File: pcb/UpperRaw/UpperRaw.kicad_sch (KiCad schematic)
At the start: 17 parts, among them J1 Conn_01x04, SW100 SW_DPDT_x2, SW101 SW_DPDT_x2, SW102 SW_SPDT, SW103 SW_SPDT

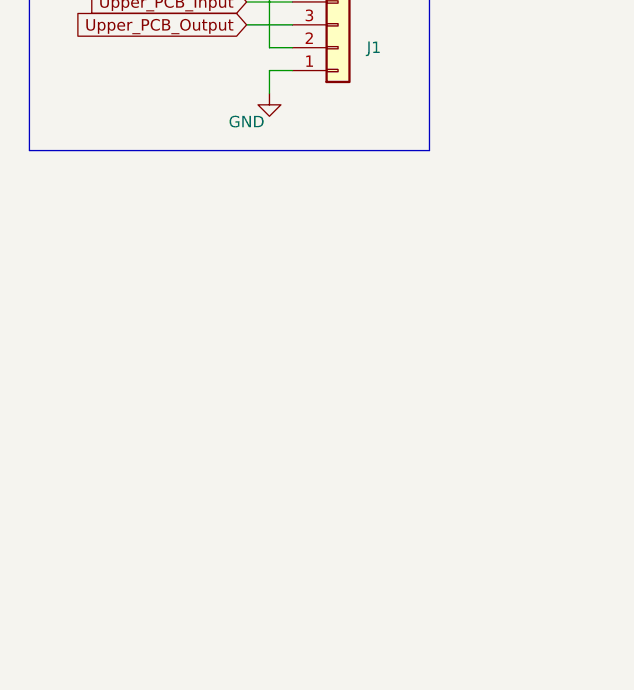
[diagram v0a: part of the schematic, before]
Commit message: [UpperRaw] Add symbols from 404 PCB
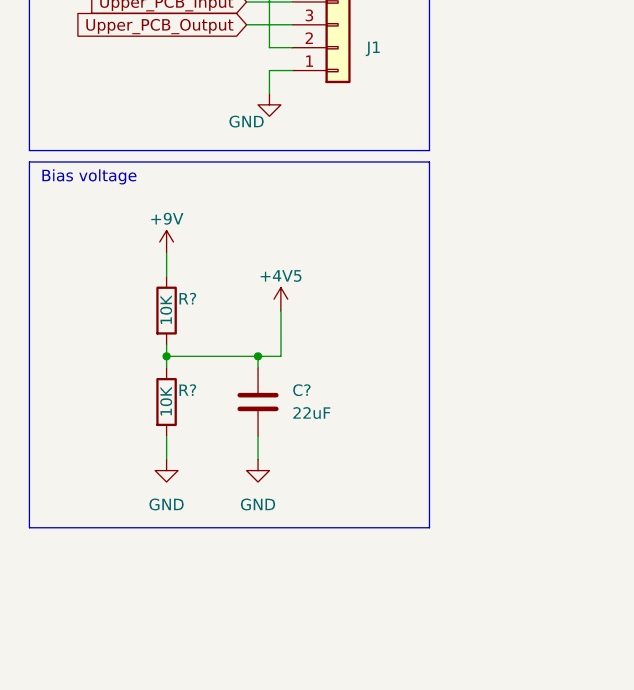
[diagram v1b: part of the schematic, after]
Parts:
- added C?: 22uF, Capacitor_SMD:C_1206_3216Metric, symbol Device:C
- added R? (x2): 10K, Resistor_SMD:R_0603_1608Metric, symbol Device:R
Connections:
- net +9V: now also R?.1
- net GND: now also C?.2, R?.2
- new net +4V5: C?.1, R?.1, R?.2
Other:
- note added: "Bias voltage"
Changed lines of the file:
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@@
     (company "Binary-6")
   )
+  (junction (at 29.21 63.5) (diameter 0) (color 0 0 0 0)
+  )
+  (junction (at 39.37 63.5) (diameter 0) (color 0 0 0 0)
+  )
   (polyline (pts (xy 58.42 40.64) (xy 58.42 13.97))
     (stroke (width 0) (type default) (color 0 0 0 0))
@@
     (stroke (width 0) (type default) (color 0 0 0 0))
   )
+  (wire (pts (xy 29.21 63.5) (xy 39.37 63.5))
+    (stroke (width 0) (type default) (color 0 0 0 0))
+  )
+  (polyline (pts (xy 13.97 82.55) (xy 58.42 82.55))
+    (stroke (width 0) (type default) (color 0 0 0 0))
+  )
   (wire (pts (xy 40.64 21.59) (xy 40.64 29.21))
     (stroke (width 0) (type default) (color 0 0 0 0))
   )
+  (wire (pts (xy 41.91 63.5) (xy 39.37 63.5))
+    (stroke (width 0) (type default) (color 0 0 0 0))
+  )
+  (wire (pts (xy 29.21 62.23) (xy 29.21 63.5))
+    (stroke (width 0) (type default) (color 0 0 0 0))
+  )
+  (wire (pts (xy 29.21 72.39) (xy 29.21 74.93))
+    (stroke (width 0) (type default) (color 0 0 0 0))
+  )
   (polyline (pts (xy 13.97 40.64) (xy 58.42 40.64))
     (stroke (width 0) (type default) (color 0 0 0 0))
   )
+  (polyline (pts (xy 13.97 41.91) (xy 13.97 82.55))
+    (stroke (width 0) (type default) (color 0 0 0 0))
+  )
   (polyline (pts (xy 58.42 13.97) (xy 13.97 13.97))
     (stroke (width 0) (type default) (color 0 0 0 0))
   )
+  (wire (pts (xy 29.21 63.5) (xy 29.21 64.77))
+    (stroke (width 0) (type default) (color 0 0 0 0))
+  )
+  (wire (pts (xy 29.21 52.07) (xy 29.21 54.61))
+    (stroke (width 0) (type default) (color 0 0 0 0))
+  )
   (polyline (pts (xy 12.7 149.86) (xy 12.7 196.85))
     (stroke (width 0) (type default) (color 0 0 0 0))
@@
     (stroke (width 0) (type default) (color 0 0 0 0))
   )
+  (wire (pts (xy 39.37 72.39) (xy 39.37 74.93))
+    (stroke (width 0) (type default) (color 0 0 0 0))
+  )
   (wire (pts (xy 40.64 31.75) (xy 40.64 34.29))
     (stroke (width 0) (type default) (color 0 0 0 0))
@@
     (stroke (width 0) (type default) (color 0 0 0 0))
   )
+  (polyline (pts (xy 58.42 41.91) (xy 58.42 82.55))
+    (stroke (width 0) (type default) (color 0 0 0 0))
+  )
+  (wire (pts (xy 41.91 58.42) (xy 41.91 63.5))
+    (stroke (width 0) (type default) (color 0 0 0 0))
+  )
   (wire (pts (xy 38.1 24.13) (xy 43.18 24.13))
     (stroke (width 0) (type default) (color 0 0 0 0))
   )
+  (wire (pts (xy 39.37 63.5) (xy 39.37 64.77))
+    (stroke (width 0) (type default) (color 0 0 0 0))
+  )
   (polyline (pts (xy 12.7 149.86) (xy 134.62 149.86))
     (stroke (width 0) (type default) (color 0 0 0 0))
   )
+  (polyline (pts (xy 58.42 41.91) (xy 13.97 41.91))
+    (stroke (width 0) (type default) (color 0 0 0 0))
+  )
   (polyline (pts (xy 134.62 149.86) (xy 134.62 196.85))
     (stroke (width 0) (type default) (color 0 0 0 0))
@@
   (polyline (pts (xy 13.97 13.97) (xy 13.97 40.64))
     (stroke (width 0) (type default) (color 0 0 0 0))
+  )
+  (text "Bias voltage" (at 15.24 44.45 0)
+    (effects (font (size 1.27 1.27)) (justify left bottom))
   )
   (text "Lower to Upper PCB connector" (at 14.605 16.51 0)
@@
     (pin "1")
   )
+  (symbol (lib_id "power:GND") (at 39.37 74.93 0) (unit 1)
+    (in_bom yes) (on_board yes)
+    (property "Reference" "#PWR?" (id 0) (at 39.37 81.28 0)
+      (effects (font (size 1.27 1.27)) hide)
+    )
+    (property "Value" "GND" (id 1) (at 39.37 80.01 0))
+    (property "Footprint" "" (id 2) (at 39.37 74.93 0)
+      (effects (font (size 1.27 1.27)) hide)
+    )
+    (property "Datasheet" "" (id 3) (at 39.37 74.93 0)
+      (effects (font (size 1.27 1.27)) hide)
+    )
+    (pin "1")
+  )
   (symbol (lib_id "Switch:SW_SPDT") (at 120.65 161.29 0) (unit 1)
     (in_bom yes) (on_board yes) (fields_autoplaced)
@@
     (pin "2")
   )
+  (symbol (lib_id "power:+9V") (at 29.21 52.07 0) (unit 1)
+    (in_bom yes) (on_board yes)
+    (property "Reference" "#PWR?" (id 0) (at 29.21 55.88 0)
+      (effects (font (size 1.27 1.27)) hide)
+    )
+    (property "Value" "+9V" (id 1) (at 29.21 48.26 0))
+    (property "Footprint" "" (id 2) (at 29.21 52.07 0)
+      (effects (font (size 1.27 1.27)) hide)
+    )
+    (property "Datasheet" "" (id 3) (at 29.21 52.07 0)
+      (effects (font (size 1.27 1.27)) hide)
+    )
+    (pin "1")
+  )
   (symbol (lib_id "Switch:SW_DPDT_x2") (at 87.63 173.99 0) (unit 2)
     (in_bom yes) (on_board yes) (fields_autoplaced)
@@
     (pin "1")
   )
+  (symbol (lib_id "Device:R") (at 29.21 58.42 0) (unit 1)
+    (in_bom yes) (on_board yes)
+    (property "Reference" "R?" (id 0) (at 30.48 57.15 0)
+      (effects (font (size 1.27 1.27)) (justify left))
+    )
+    (property "Value" "10K" (id 1) (at 29.21 58.42 90))
+    (property "Footprint" "Resistor_SMD:R_0603_1608Metric" (id 2) (at 27.432 58.42 90)
+      (effects (font (size 1.27 1.27)) hide)
+    )
+    (property "Datasheet" "~" (id 3) (at 29.21 58.42 0)
+      (effects (font (size 1.27 1.27)) hide)
+    )
+    (property "LCSC" "C25804" (id 4) (at 29.21 58.42 0)
+      (effects (font (size 1.27 1.27)) hide)
+    )
+    (pin "1")
+    (pin "2")
+  )
   (symbol (lib_id "Device:C") (at 36.83 180.34 0) (mirror y) (unit 1)
     (in_bom yes) (on_board yes) (fields_autoplaced)
@@
     (pin "2")
   )
+  (symbol (lib_id "Device:C") (at 39.37 68.58 0) (unit 1)
+    (in_bom yes) (on_board yes) (fields_autoplaced)
+    (property "Reference" "C?" (id 0) (at 43.18 67.3099 0)
+      (effects (font (size 1.27 1.27)) (justify left))
+    )
+    (property "Value" "22uF" (id 1) (at 43.18 69.8499 0)
+      (effects (font (size 1.27 1.27)) (justify left))
+    )
+    (property "Footprint" "Capacitor_SMD:C_1206_3216Metric" (id 2) (at 40.3352 72.39 0)
+      (effects (font (size 1.27 1.27)) hide)
+    )
+    (property "Datasheet" "~" (id 3) (at 39.37 68.58 0)
+      (effects (font (size 1.27 1.27)) hide)
+    )
+    (property "LCSC" "C12891" (id 4) (at 39.37 68.58 0)
+      (effects (font (size 1.27 1.27)) hide)
+    )
+    (pin "1")
+    (pin "2")
+  )
+  (symbol (lib_id "Device:R") (at 29.21 68.58 0) (unit 1)
+    (in_bom yes) (on_board yes)
+    (property "Reference" "R?" (id 0) (at 30.48 67.31 0)
+      (effects (font (size 1.27 1.27)) (justify left))
+    )
+    (property "Value" "10K" (id 1) (at 29.21 68.58 90))
+    (property "Footprint" "Resistor_SMD:R_0603_1608Metric" (id 2) (at 27.432 68.58 90)
+      (effects (font (size 1.27 1.27)) hide)
+    )
+    (property "Datasheet" "~" (id 3) (at 29.21 68.58 0)
+      (effects (font (size 1.27 1.27)) hide)
+    )
+    (property "LCSC" "C25804" (id 4) (at 29.21 68.58 0)
+      (effects (font (size 1.27 1.27)) hide)
+    )
+    (pin "1")
+    (pin "2")
+  )
   (symbol (lib_id "power:+9V") (at 16.51 162.56 0) (unit 1)
     (in_bom yes) (on_board yes)
@@
     (pin "1")
     (pin "2")
+  )
+  (symbol (lib_id "power:GND") (at 29.21 74.93 0) (unit 1)
+    (in_bom yes) (on_board yes)
+    (property "Reference" "#PWR?" (id 0) (at 29.21 81.28 0)
+      (effects (font (size 1.27 1.27)) hide)
+    )
+    (property "Value" "GND" (id 1) (at 29.21 80.01 0))
+    (property "Footprint" "" (id 2) (at 29.21 74.93 0)
+      (effects (font (size 1.27 1.27)) hide)
+    )
+    (property "Datasheet" "" (id 3) (at 29.21 74.93 0)
+      (effects (font (size 1.27 1.27)) hide)
+    )
+    (pin "1")
+  )
+  (symbol (lib_id "MeineBibli:+4V5") (at 41.91 58.42 0) (unit 1)
+    (in_bom yes) (on_board yes)
+    (property "Reference" "#PWR?" (id 0) (at 41.91 62.23 0)
+      (effects (font (size 1.27 1.27)) hide)
+    )
+    (property "Value" "+4V5" (id 1) (at 41.91 54.61 0))
+    (property "Footprint" "" (id 2) (at 41.91 58.42 0)
+      (effects (font (size 1.27 1.27)) hide)
+    )
+    (property "Datasheet" "" (id 3) (at 41.91 58.42 0)
+      (effects (font (size 1.27 1.27)) hide)
+    )
+    (pin "1")
   )
   (symbol (lib_id "power:GND") (at 16.51 168.91 0) (unit 1)
@@
       (reference "#PWR04") (unit 1) (value "GND") (footprint "")
     )
+    (path "/09433d97-62ec-42de-89f2-7d0b68dc1b9d"
+      (reference "#PWR?") (unit 1) (value "GND") (footprint "")
+    )
+    (path "/296b967f-b7a9-453f-856a-7b874fdca3db"
+      (reference "#PWR?") (unit 1) (value "+9V") (footprint "")
+    )
+    (path "/b9272e8b-2d00-4d6b-ae8c-fd62ef331586"
+      (reference "#PWR?") (unit 1) (value "GND") (footprint "")
+    )
+    (path "/c2d81a3b-9b02-4ddc-9c7b-c0e881678970"
+      (reference "#PWR?") (unit 1) (value "+4V5") (footprint "")
+    )
     (path "/75f89342-e5fb-4ec8-a9a1-4514a000c1c5"
       (reference "C100") (unit 1) (value "100uF") (footprint "Capacitor_THT:CP_Radial_D5.0mm_P2.00mm")
@@
       (reference "C102") (unit 1) (value "220nF") (footprint "Capacitor_SMD:C_0603_1608Metric")
     )
+    (path "/8672a05d-b750-4ddd-a92d-4c58fddcdd4e"
+      (reference "C?") (unit 1) (value "22uF") (footprint "Capacitor_SMD:C_1206_3216Metric")
+    )
     (path "/43624bd7-5b28-4455-bedf-a59e39f0128d"
       (reference "J1") (unit 1) (value "Conn_01x04") (footprint "Connector_JST:JST_XH_B4B-XH-A_1x04_P2.50mm_Vertical")
@@
       (reference "R103") (unit 1) (value "2k2") (footprint "Resistor_SMD:R_0603_1608Metric")
     )
+    (path "/4e944601-14c5-4478-a9d6-8d2ad19dcc43"
+      (reference "R?") (unit 1) (value "10K") (footprint "Resistor_SMD:R_0603_1608Metric")
+    )
+    (path "/8d9ea4cf-1047-42af-bf72-13258f22d6ad"
+      (reference "R?") (unit 1) (value "10K") (footprint "Resistor_SMD:R_0603_1608Metric")
+    )
     (path "/eade452d-0fd2-478e-ba2c-c8c7cc57b518"

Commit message: [All] Add LCSC part number for JST connector
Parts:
- J1: value Conn_01x04 -> (none); footprint Connector_JST:JST_XH_B4B-XH-A_1x04_P2.50mm_Vertical -> (none); LCSC (none) -> C144395; now in the parts list
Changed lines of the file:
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@@
     (pin "2")
     (pin "3")
+    (pin "4")
+    (pin "5")
+    (pin "6")
   )
   (symbol (lib_id "Device:R") (at 50.8 180.34 0) (unit 1)
@@
       (effects (font (size 1.27 1.27)) hide)
     )
+    (pin "1")
+    (pin "2")
+    (pin "3")
     (pin "4")
     (pin "5")
@@
   )
   (symbol (lib_id "Connector_Generic:Conn_01x04") (at 48.26 29.21 0) (mirror x) (unit 1)
-    (in_bom no) (on_board yes)
+    (in_bom yes) (on_board yes)
     (property "Reference" "J1" (id 0) (at 51.435 29.2101 0)
       (effects (font (size 1.27 1.27)) (justify left))
     )
-    (property "Value" "Conn_01x04" (id 1) (at 44.45 21.59 0)
-      (effects (font (size 1.27 1.27)) (justify left))
-    )
-    (property "Footprint" "Connector_JST:JST_XH_B4B-XH-A_1x04_P2.50mm_Vertical" (id 2) (at 48.26 29.21 0)
+    (property "Value" "" (id 1) (at 44.45 21.59 0)
+      (effects (font (size 1.27 1.27)) (justify left))
+    )
+    (property "Footprint" "" (id 2) (at 48.26 29.21 0)
       (effects (font (size 1.27 1.27)) hide)
     )
     (property "Datasheet" "~" (id 3) (at 48.26 29.21 0)
+      (effects (font (size 1.27 1.27)) hide)
+    )
+    (property "LCSC" "C144395" (id 4) (at 48.26 29.21 0)
       (effects (font (size 1.27 1.27)) hide)
     )
@@
       (effects (font (size 1.27 1.27)) hide)
     )
+    (pin "1")
+    (pin "2")
+    (pin "3")
     (pin "4")
     (pin "5")
@@
     (pin "2")
     (pin "3")
+    (pin "4")
+    (pin "5")
+    (pin "6")
   )
   (symbol (lib_id "power:+9V") (at 40.64 21.59 0) (unit 1)

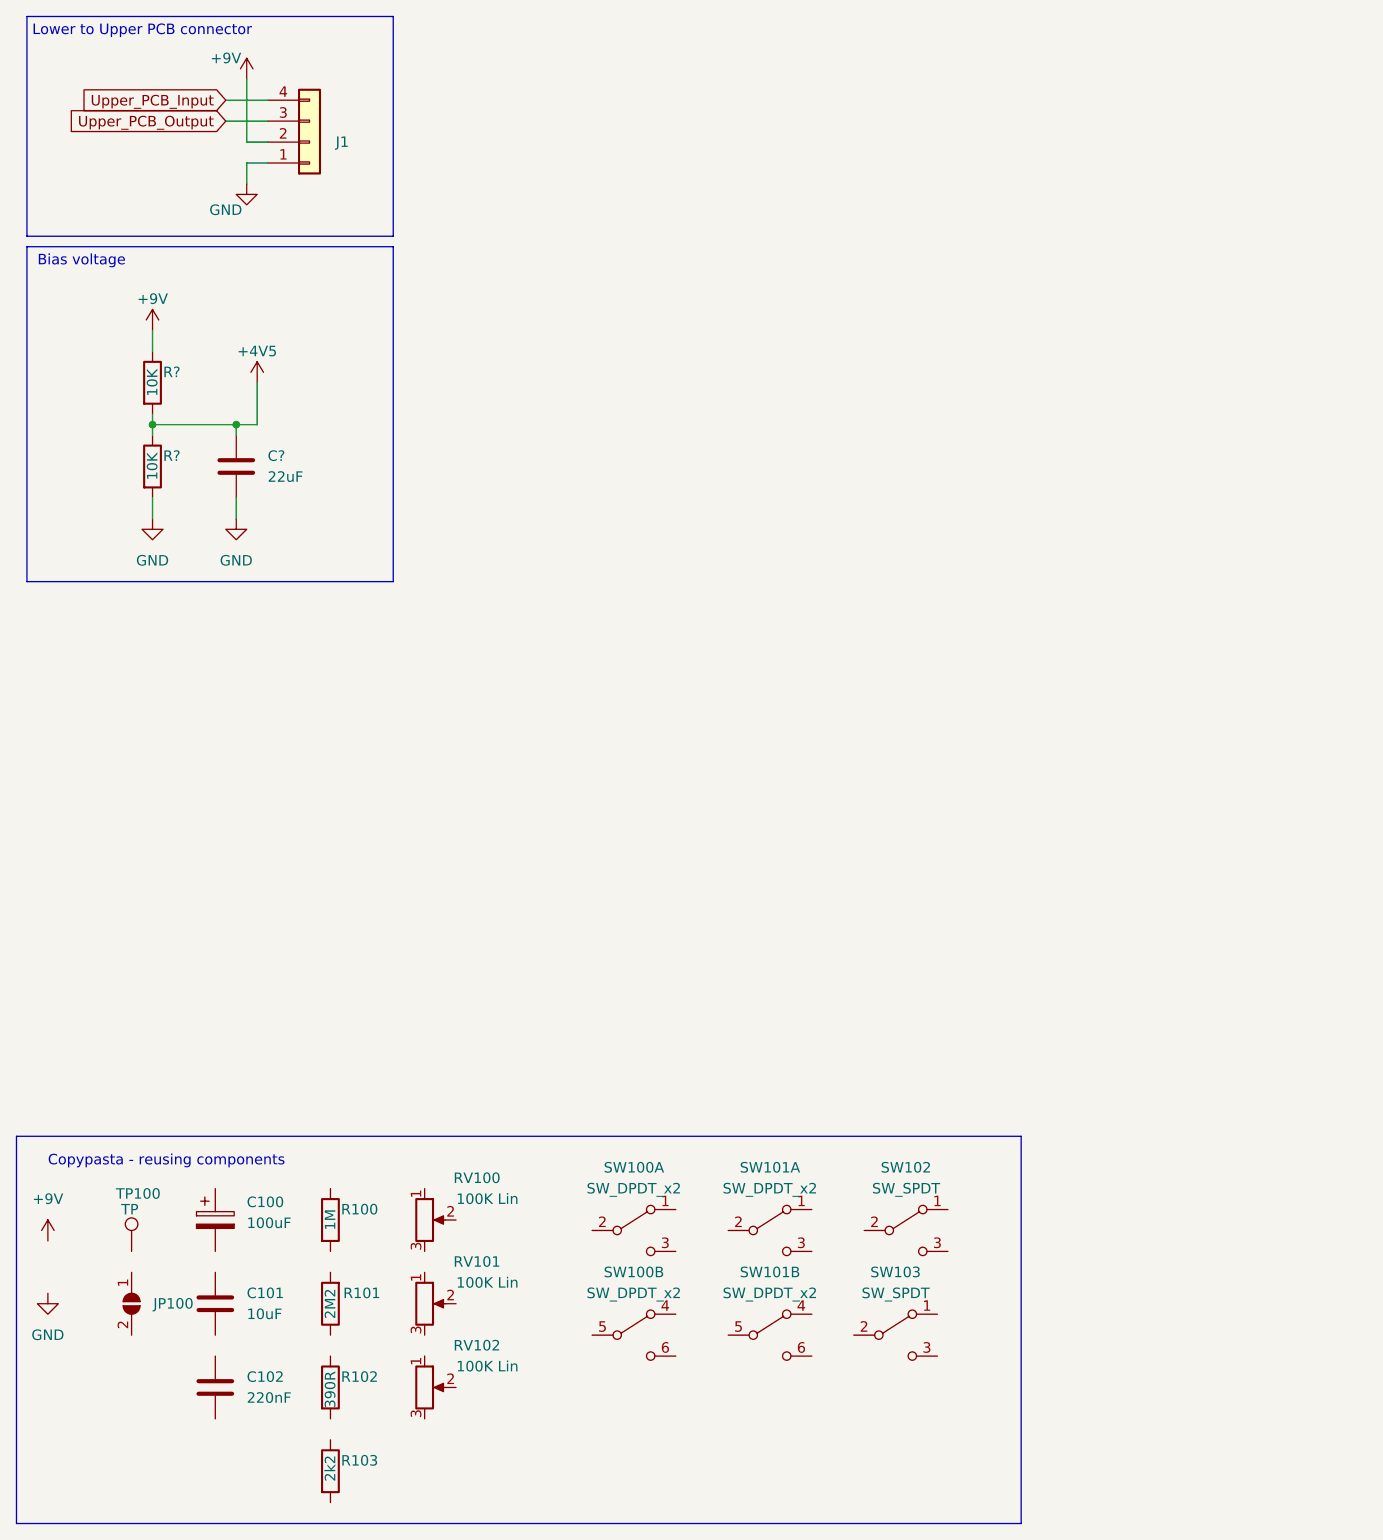
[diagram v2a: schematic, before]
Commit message: [UpperRaw] Figure out new pot positions for 6 pots
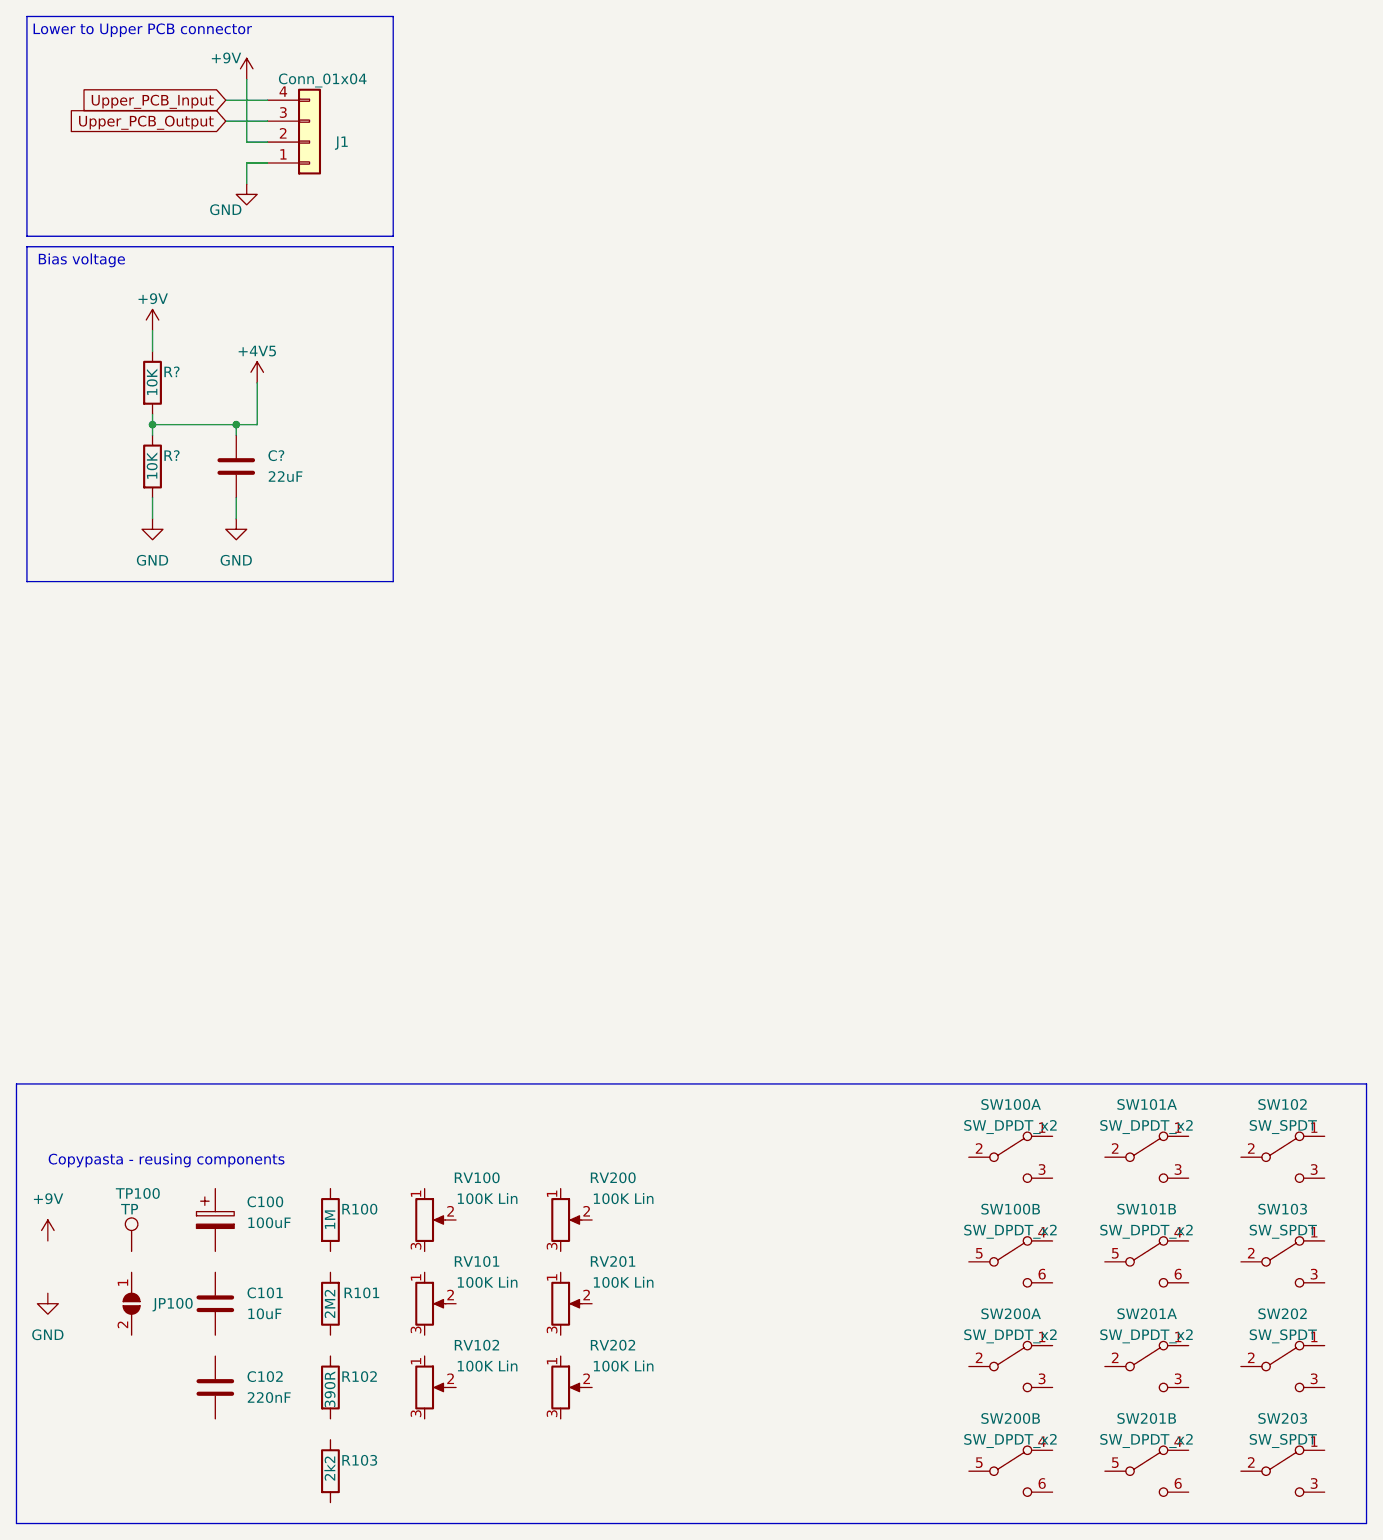
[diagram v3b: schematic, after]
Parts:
- added RV200, RV201, RV202: 100K Lin, Potentiometer_THT:Potentiometer_Alpha_RD901F-40-00D_Single_Vertical, symbol Device:R_Potentiometer
- added SW200, SW201: SW_DPDT_x2, MeineBib:Switch_toggle_DPDT_Print, symbol Switch:SW_DPDT_x2
- added SW202, SW203: SW_SPDT, MeineBib:Switch_toggle_SPDT_Print, symbol Switch:SW_SPDT
- J1: value (none) -> Conn_01x04; footprint (none) -> Connector_JST:JST_XH_B4B-XH-A_1x04_P2.50mm_Vertical
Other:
- moved on the sheet: SW100A, SW100B, SW101A, SW101B, SW102, SW103
